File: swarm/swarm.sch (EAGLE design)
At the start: 6 parts

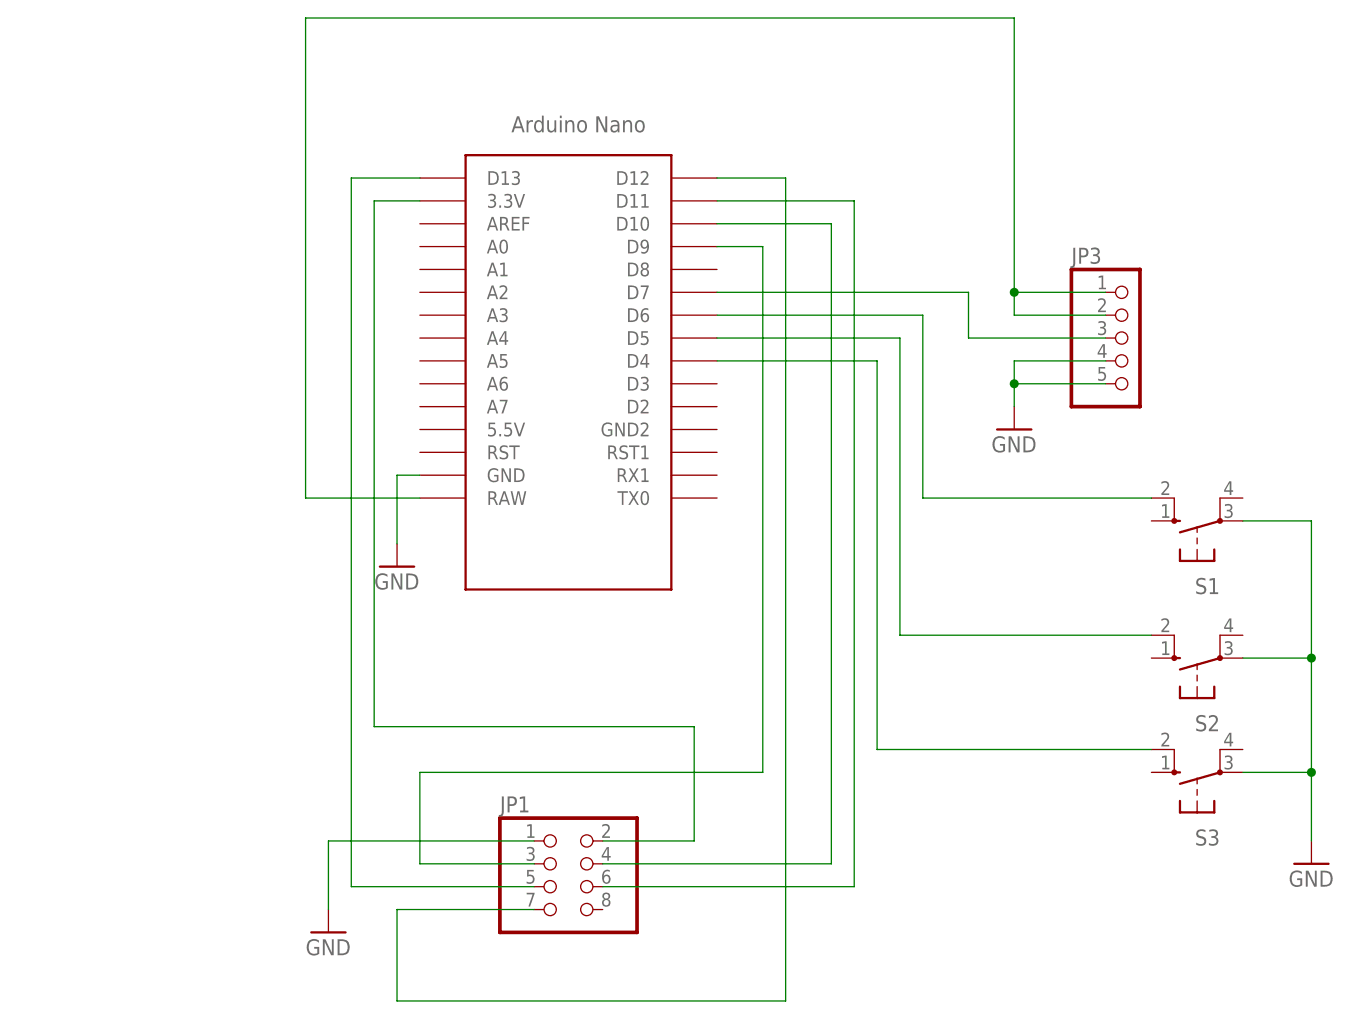
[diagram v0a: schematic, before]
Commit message: Add files via upload
added accelerator connector
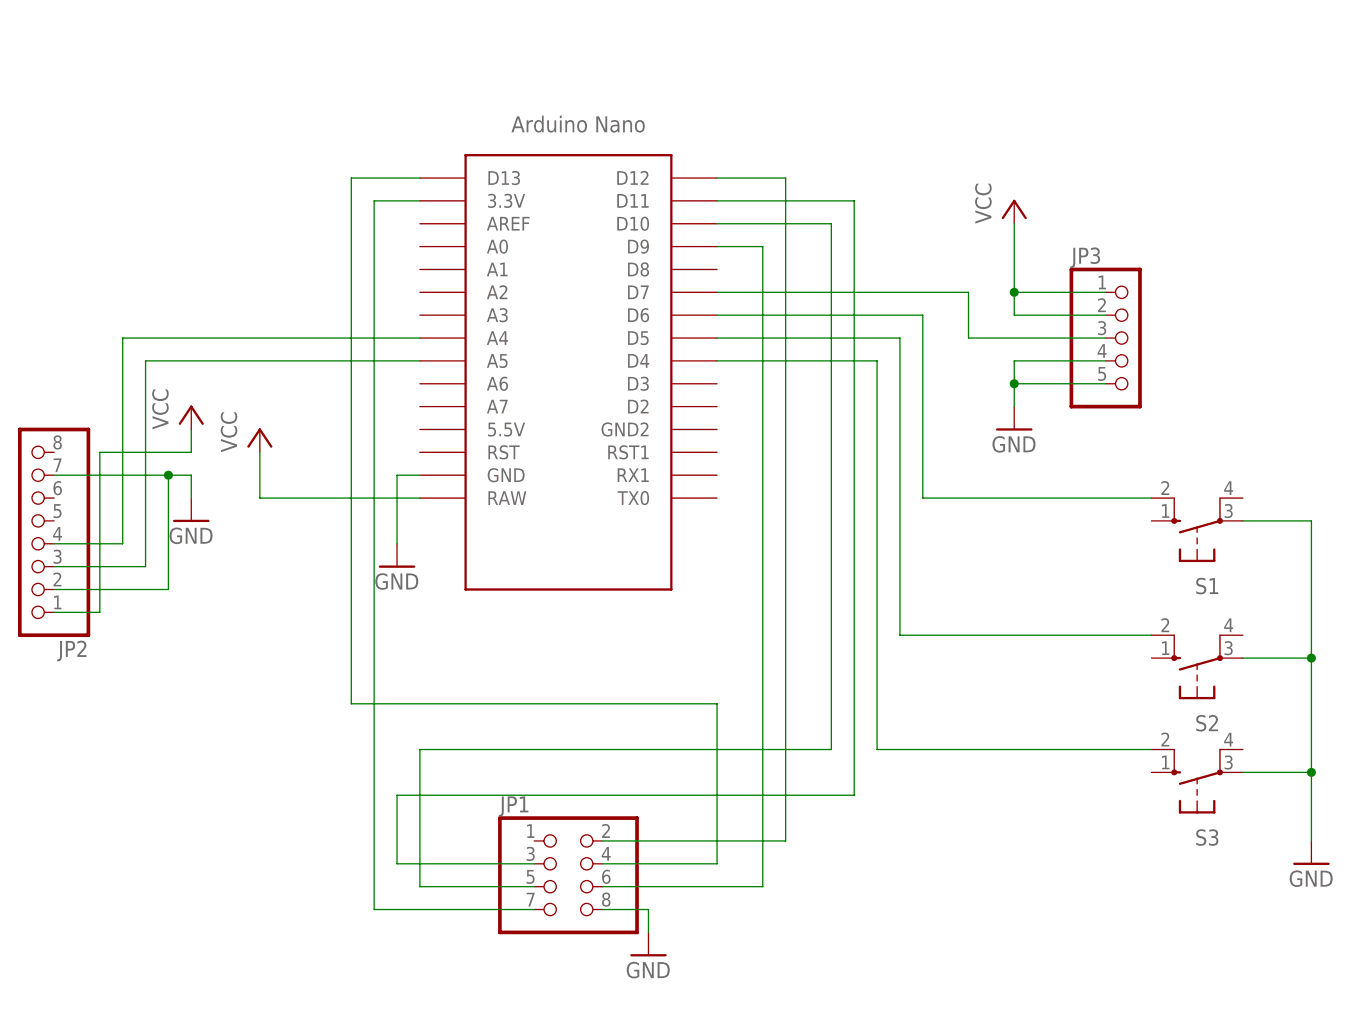
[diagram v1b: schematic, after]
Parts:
- added JP2: (no value), pinhead:PINHD-1X8
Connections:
- new net N$12: JP1.2, U$1.D12
- new net VCC: JP2.1, JP3.1, JP3.2, U$1.RAW
- net GND: now also JP1.8, JP2.2, JP2.7; no longer JP1.1
- net N$2: now also JP2.3, U$1.A5; no longer JP3.1, JP3.2, U$1.RAW
- net N$4: now also JP2.4, U$1.A4; no longer JP1.7, U$1.D12
- net N$5: now also JP1.4; no longer JP1.5
- net N$6: now also JP1.6; no longer JP1.3
- net N$7: now also JP1.3; no longer JP1.6
- net N$8: now also JP1.5; no longer JP1.4
- net N$9: now also JP1.7; no longer JP1.2
